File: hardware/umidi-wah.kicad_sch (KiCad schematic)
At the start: 70 parts

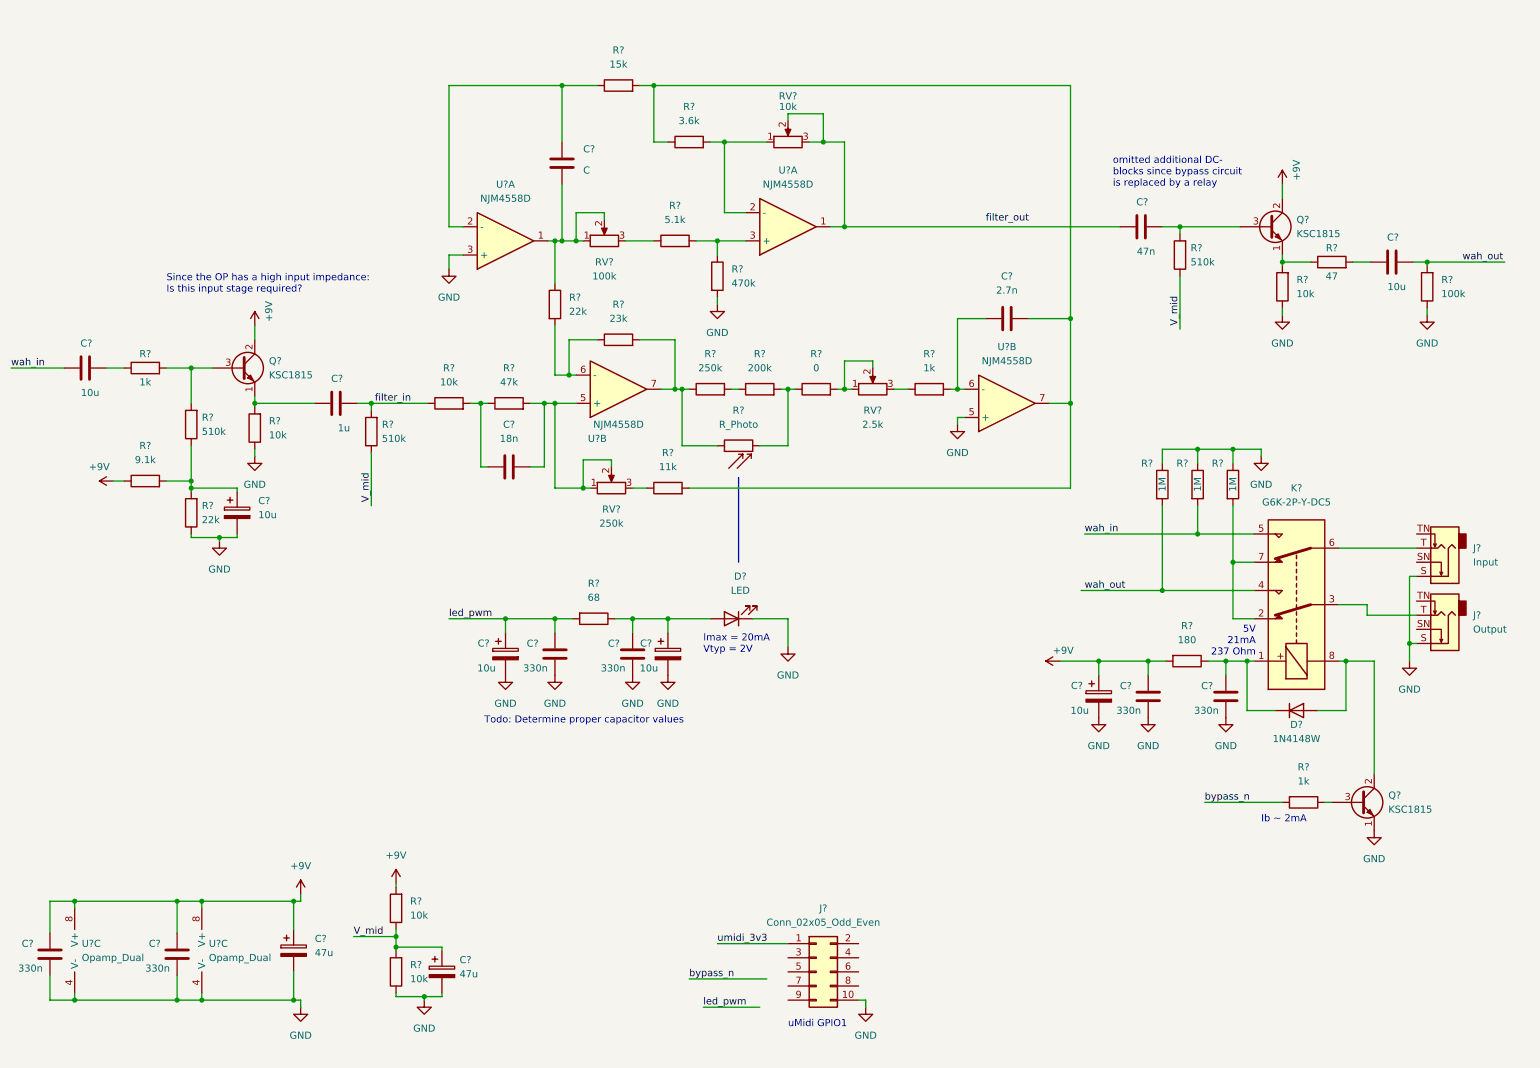
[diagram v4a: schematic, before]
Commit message: Add power input and 5v ldo for umidi supply
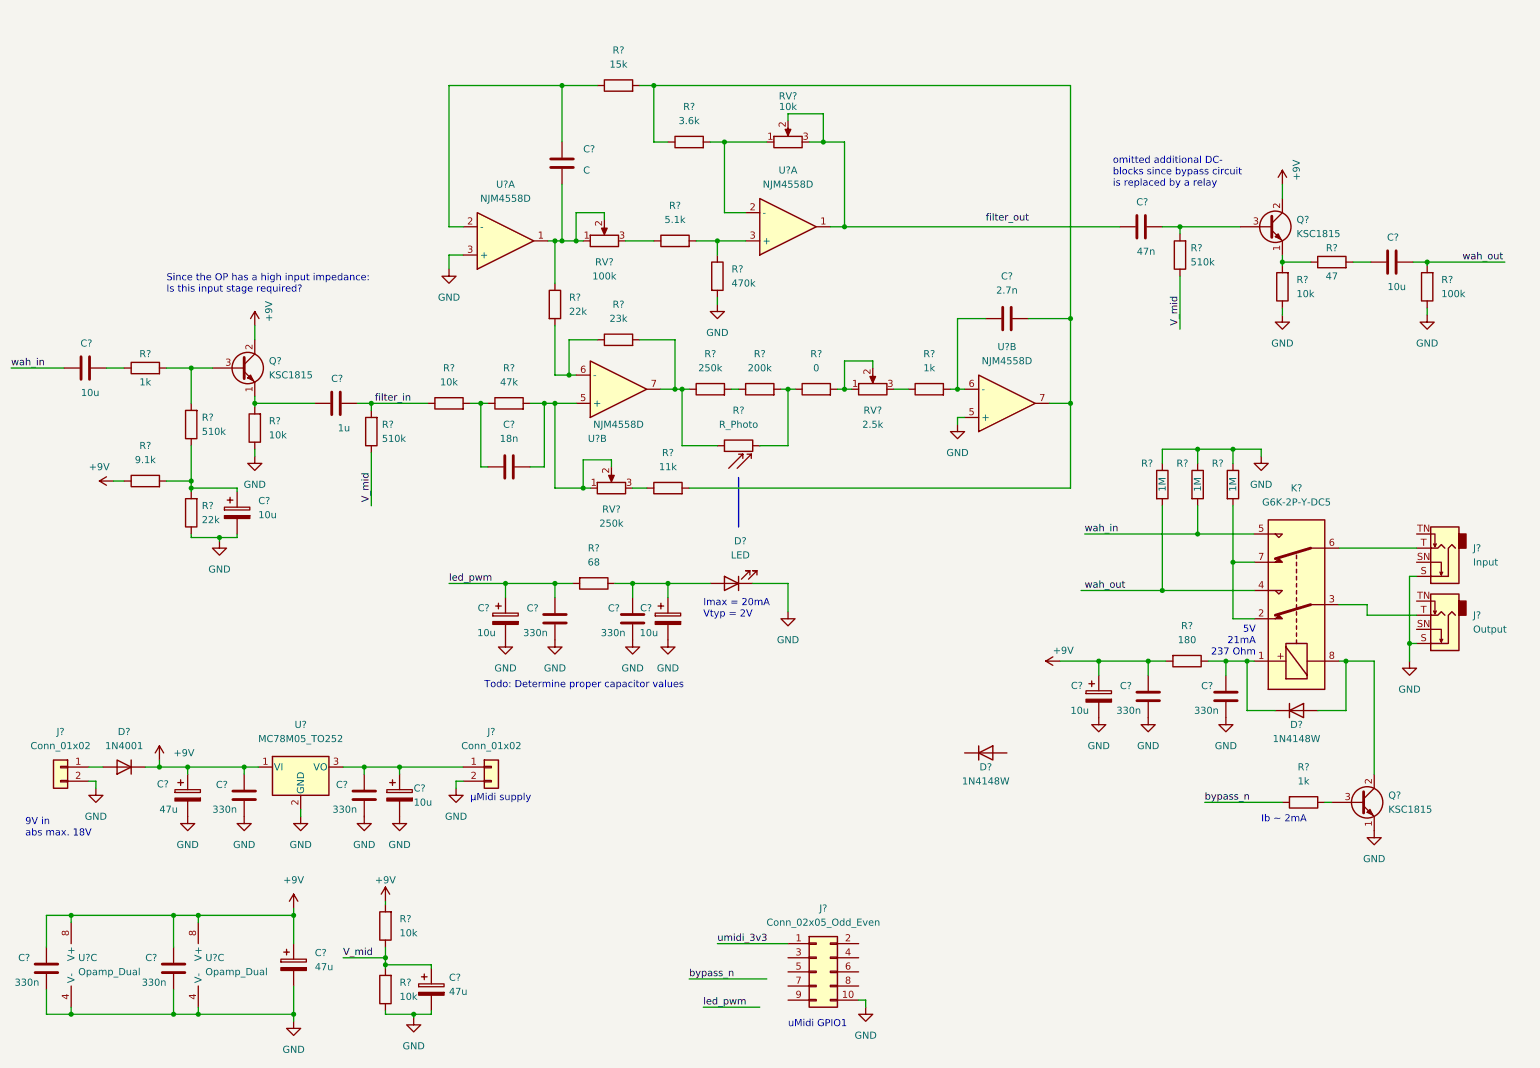
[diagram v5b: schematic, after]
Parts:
- added C? (x2): 330n, symbol Device:C
- added C?: 10u, symbol Device:C_Polarized
- added C?: 47u, symbol Device:C_Polarized
- added D?: 1N4001, Diode_THT:D_DO-41_SOD81_P10.16mm_Horizontal, symbol Diode:1N4001
- added D?: 1N4148W, Diode_SMD:D_SOD-123, symbol Diode:1N4148W
- added J? (x2): Conn_01x02, symbol Connector_Generic:Conn_01x02
- added U?: MC78M05_TO252, Package_TO_SOT_SMD:TO-252-2, symbol Regulator_Linear:MC78M05_TO252
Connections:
- net +9V: now also C?.1, C?.1, D?.1 (K), U?.1 (VI)
- net GND: now also C?.2, C?.2, C?.2, C?.2, J?.2 (Pin_2), J?.2 (Pin_2), U?.2 (GND)
- new net: C?.1, C?.1, J?.1 (Pin_1), U?.3 (VO)
- new net: D?.2 (A), J?.1 (Pin_1)
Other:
- note added: "9V in abs max. 18V"
- note added: "μMidi supply"
- moved on the sheet: C?, D?, R?, U?C

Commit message: Add buffer stage bypass resistors
Can be assembled to bypass input or output buffer stages.
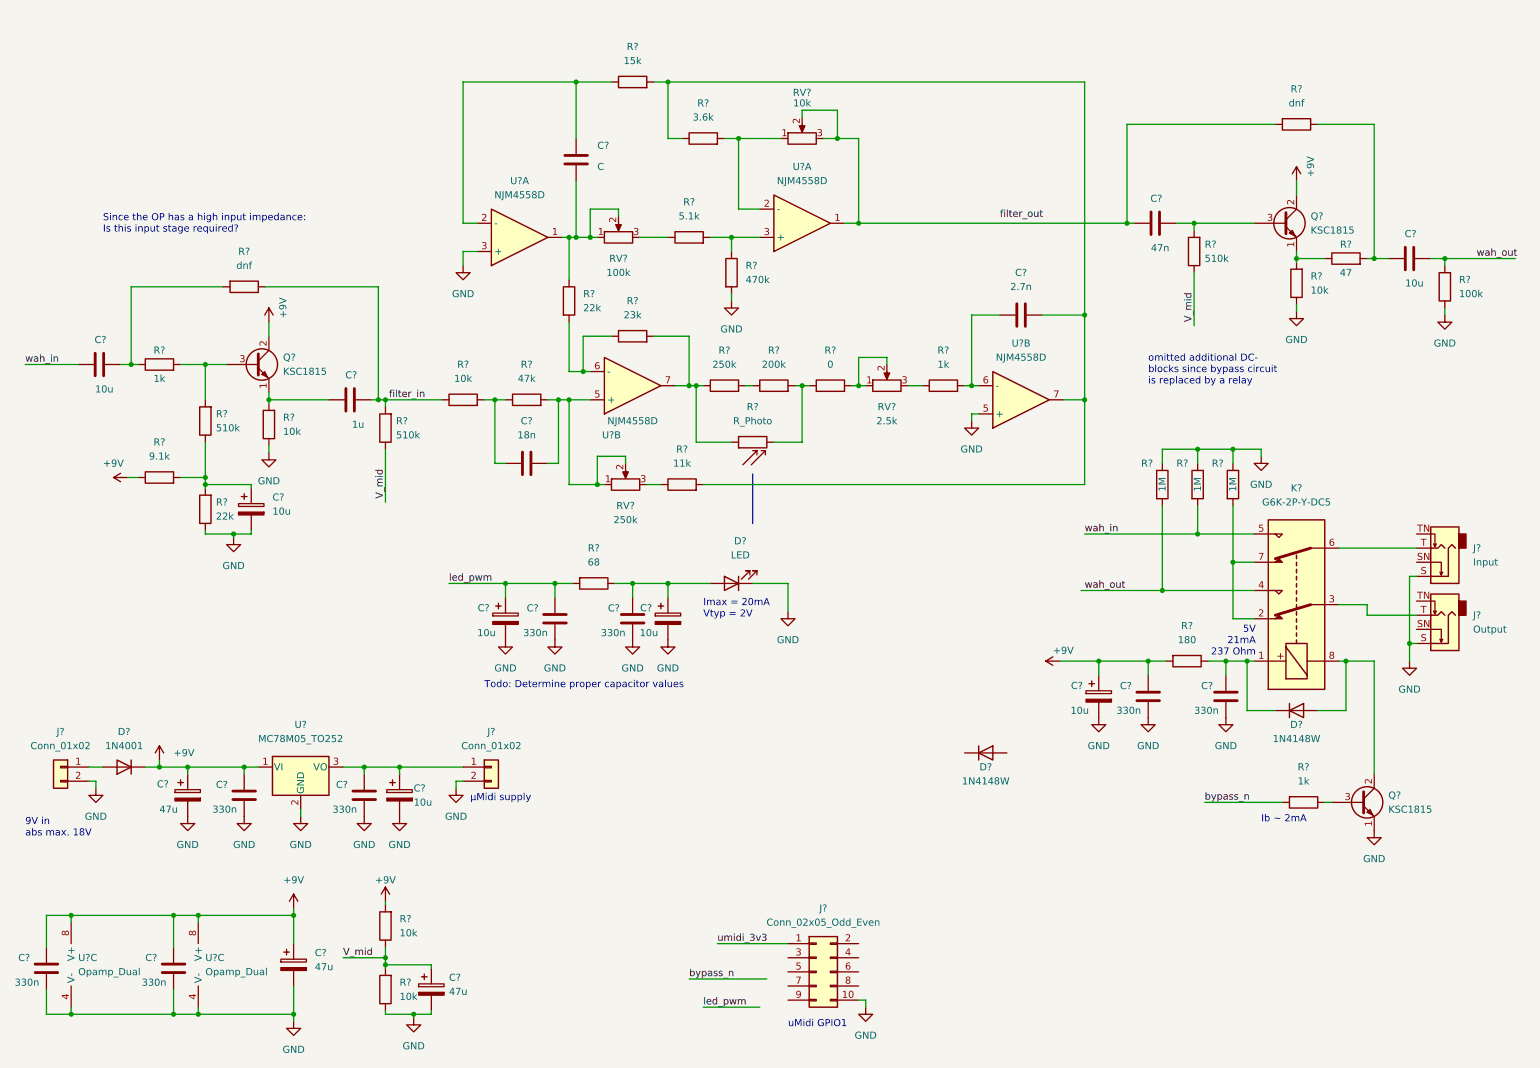
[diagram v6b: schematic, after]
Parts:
- added R? (x2): dnf, symbol Device:R
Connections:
- net filter_in: now also R?.1
- net at C?.1, RV?.2, RV?.3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: now also R?.2
- net at C?.1, R?.2: now also R?.1
- net at C?.2, R?.1: now also R?.2
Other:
- moved on the sheet: C?, Q?, R?, RV?, U?A, U?B

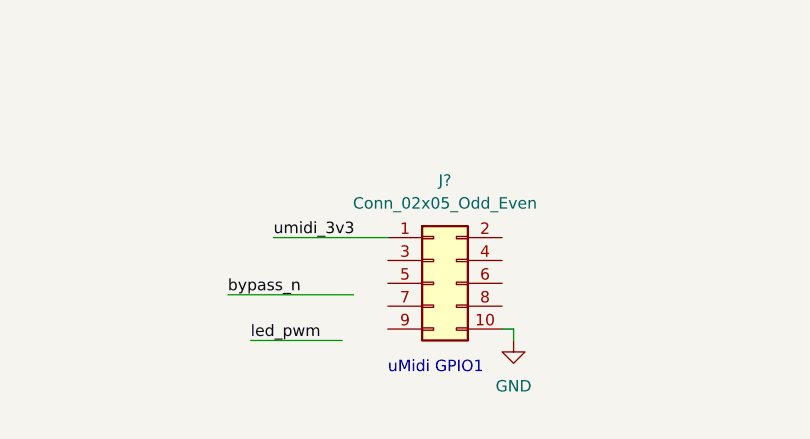
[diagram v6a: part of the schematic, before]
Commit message: Use gpio pinout from current uMidi wah app
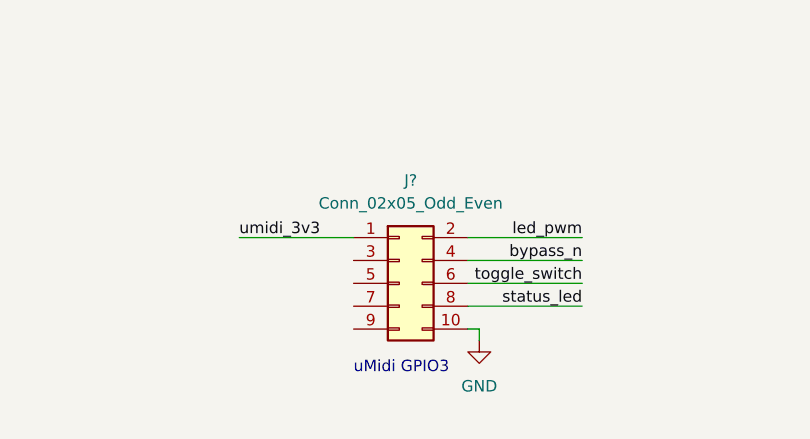
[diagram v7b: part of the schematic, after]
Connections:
- net bypass_n: now also J?.4 (Pin_4)
- net led_pwm: now also J?.2 (Pin_2)
- net toggle_switch: now reaches J?.6 (Pin_6)
- net status_led: now reaches J?.8 (Pin_8)
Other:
- note added: "uMidi GPIO3"
- note removed: "uMidi GPIO1"
- moved on the sheet: J?
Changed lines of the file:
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@@
-    (stroke (width 0) (type default) (color 0 0 0 0))
-  )
-  (wire (pts (xy 134.62 184.15) (xy 148.59 184.15))
     (stroke (width 0) (type default) (color 0 0 0 0))
   )
@@
     (stroke (width 0) (type default) (color 0 0 0 0))
   )
-  (wire (pts (xy 165.1 187.96) (xy 166.37 187.96))
+  (wire (pts (xy 161.29 187.96) (xy 162.56 187.96))
     (stroke (width 0) (type default) (color 0 0 0 0))
   )
@@
     (stroke (width 0) (type default) (color 0 0 0 0))
   )
+  (wire (pts (xy 161.29 185.42) (xy 173.99 185.42))
+    (stroke (width 0) (type default) (color 0 0 0 0))
+  )
   (wire (pts (xy 201.93 80.01) (xy 205.74 80.01))
     (stroke (width 0) (type default) (color 0 0 0 0))
@@
     (stroke (width 0) (type default) (color 0 0 0 0))
   )
-  (wire (pts (xy 137.16 189.23) (xy 147.32 189.23))
-    (stroke (width 0) (type default) (color 0 0 0 0))
-  )
   (wire (pts (xy 264.16 111.76) (xy 264.16 123.825))
     (stroke (width 0) (type default) (color 0 0 0 0))
@@
     (stroke (width 0) (type default) (color 0 0 0 0))
   )
+  (wire (pts (xy 161.29 182.88) (xy 173.99 182.88))
+    (stroke (width 0) (type default) (color 0 0 0 0))
+  )
   (wire (pts (xy 52.705 104.14) (xy 55.88 104.14))
     (stroke (width 0) (type default) (color 0 0 0 0))
@@
     (stroke (width 0) (type default) (color 0 0 0 0))
   )
-  (wire (pts (xy 139.7 177.8) (xy 152.4 177.8))
+  (wire (pts (xy 135.89 177.8) (xy 148.59 177.8))
     (stroke (width 0) (type default) (color 0 0 0 0))
   )
@@
     (stroke (width 0) (type default) (color 0 0 0 0))
   )
+  (wire (pts (xy 161.29 180.34) (xy 173.99 180.34))
+    (stroke (width 0) (type default) (color 0 0 0 0))
+  )
   (wire (pts (xy 114.3 22.86) (xy 114.3 33.02))
     (stroke (width 0) (type default) (color 0 0 0 0))
@@
     (stroke (width 0) (type default) (color 0 0 0 0))
   )
-  (wire (pts (xy 166.37 187.96) (xy 166.37 189.23))
+  (wire (pts (xy 162.56 187.96) (xy 162.56 189.23))
     (stroke (width 0) (type default) (color 0 0 0 0))
   )
@@
   )
   (wire (pts (xy 144.78 77.47) (xy 146.05 77.47))
+    (stroke (width 0) (type default) (color 0 0 0 0))
+  )
+  (wire (pts (xy 161.29 177.8) (xy 173.99 177.8))
     (stroke (width 0) (type default) (color 0 0 0 0))
   )
@@
     (effects (font (size 1.27 1.27)) (justify left bottom))
   )
-  (text "uMidi GPIO1" (at 152.4 193.04 0)
+  (text "uMidi GPIO3" (at 148.59 193.04 0)
     (effects (font (size 1.27 1.27)) (justify left bottom))
   )
@@
     (effects (font (size 1.27 1.27)) (justify left bottom))
   )
+  (label "toggle_switch" (at 173.99 182.88 180)
+    (effects (font (size 1.27 1.27)) (justify right bottom))
+  )
   (label "wah_in" (at 15.24 73.66 0)
     (effects (font (size 1.27 1.27)) (justify left bottom))
   )
+  (label "status_led" (at 173.99 185.42 180)
+    (effects (font (size 1.27 1.27)) (justify right bottom))
+  )
   (label "filter_in" (at 80.645 80.01 0)
     (effects (font (size 1.27 1.27)) (justify left bottom))
@@
     (effects (font (size 1.27 1.27)) (justify left bottom))
   )
-  (label "umidi_3v3" (at 139.7 177.8 0)
+  (label "umidi_3v3" (at 135.89 177.8 0)
     (effects (font (size 1.27 1.27)) (justify left bottom))
   )
-  (label "led_pwm" (at 137.16 189.23 0)
-    (effects (font (size 1.27 1.27)) (justify left bottom))
+  (label "led_pwm" (at 173.99 177.8 180)
+    (effects (font (size 1.27 1.27)) (justify right bottom))
   )
   (label "filter_out" (at 190.5 47.625 0)
     (effects (font (size 1.27 1.27)) (justify left bottom))
   )
-  (label "bypass_n" (at 134.62 184.15 0)
-    (effects (font (size 1.27 1.27)) (justify left bottom))
+  (label "bypass_n" (at 173.99 180.34 180)
+    (effects (font (size 1.27 1.27)) (justify right bottom))
   )
   (label "V_mid" (at 225.425 66.04 90)
@@
     (pin "2")
   )
-  (symbol (lib_id "Connector_Generic:Conn_02x05_Odd_Even") (at 157.48 182.88 0) (unit 1)
-    (in_bom yes) (on_board yes) (fields_autoplaced)
-    (property "Reference" "J?" (id 0) (at 158.75 171.45 0))
-    (property "Value" "Conn_02x05_Odd_Even" (id 1) (at 158.75 173.99 0))
-    (property "Footprint" "Connector_IDC:IDC-Header_2x05_P2.54mm_Vertical" (id 2) (at 157.48 182.88 0)
-      (effects (font (size 1.27 1.27)) hide)
-    )
-    (property "Datasheet" "~" (id 3) (at 157.48 182.88 0)
+  (symbol (lib_id "Connector_Generic:Conn_02x05_Odd_Even") (at 153.67 182.88 0) (unit 1)
+    (in_bom yes) (on_board yes) (fields_autoplaced)
+    (property "Reference" "J?" (id 0) (at 154.94 171.45 0))
+    (property "Value" "Conn_02x05_Odd_Even" (id 1) (at 154.94 173.99 0))
+    (property "Footprint" "Connector_IDC:IDC-Header_2x05_P2.54mm_Vertical" (id 2) (at 153.67 182.88 0)
+      (effects (font (size 1.27 1.27)) hide)
+    )
+    (property "Datasheet" "~" (id 3) (at 153.67 182.88 0)
       (effects (font (size 1.27 1.27)) hide)
     )
@@
     (pin "2")
   )
-  (symbol (lib_id "power:GND") (at 166.37 189.23 0) (unit 1)
-    (in_bom yes) (on_board yes) (fields_autoplaced)
-    (property "Reference" "#PWR?" (id 0) (at 166.37 195.58 0)
-      (effects (font (size 1.27 1.27)) hide)
-    )
-    (property "Value" "GND" (id 1) (at 166.37 194.31 0))
-    (property "Footprint" "" (id 2) (at 166.37 189.23 0)
-      (effects (font (size 1.27 1.27)) hide)
-    )
-    (property "Datasheet" "" (id 3) (at 166.37 189.23 0)
-      (effects (font (size 1.27 1.27)) hide)
-    )
+  (symbol (lib_id "power:GND") (at 162.56 189.23 0) (unit 1)
+    (in_bom yes) (on_board yes) (fields_autoplaced)
+    (property "Reference" "#PWR?" (id 0) (at 162.56 195.58 0)
+      (effects (font (size 1.27 1.27)) hide)
+    )
+    (property "Value" "GND" (id 1) (at 162.56 194.31 0))
+    (property "Footprint" "" (id 2) (at 162.56 189.23 0)
+      (effects (font (size 1.27 1.27)) hide)
+    )
+    (property "Datasheet" "" (id 3) (at 162.56 189.23 0)
+      (effects (font (size 1.27 1.27)) hide)
+    )

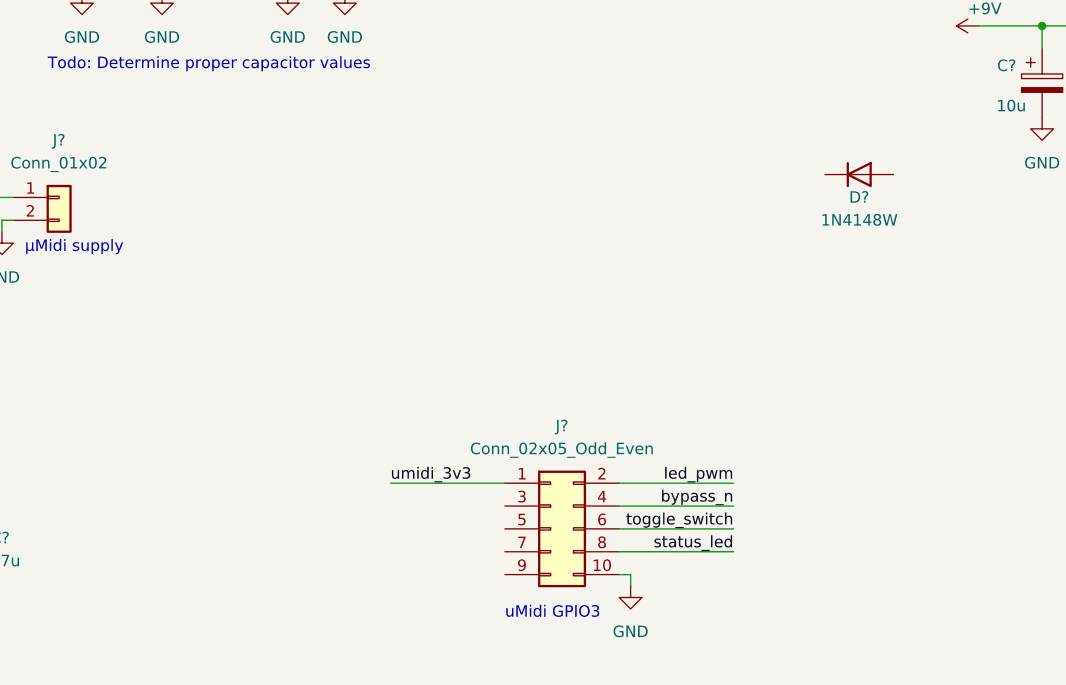
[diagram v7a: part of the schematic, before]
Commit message: Add status led and toggle switch connector
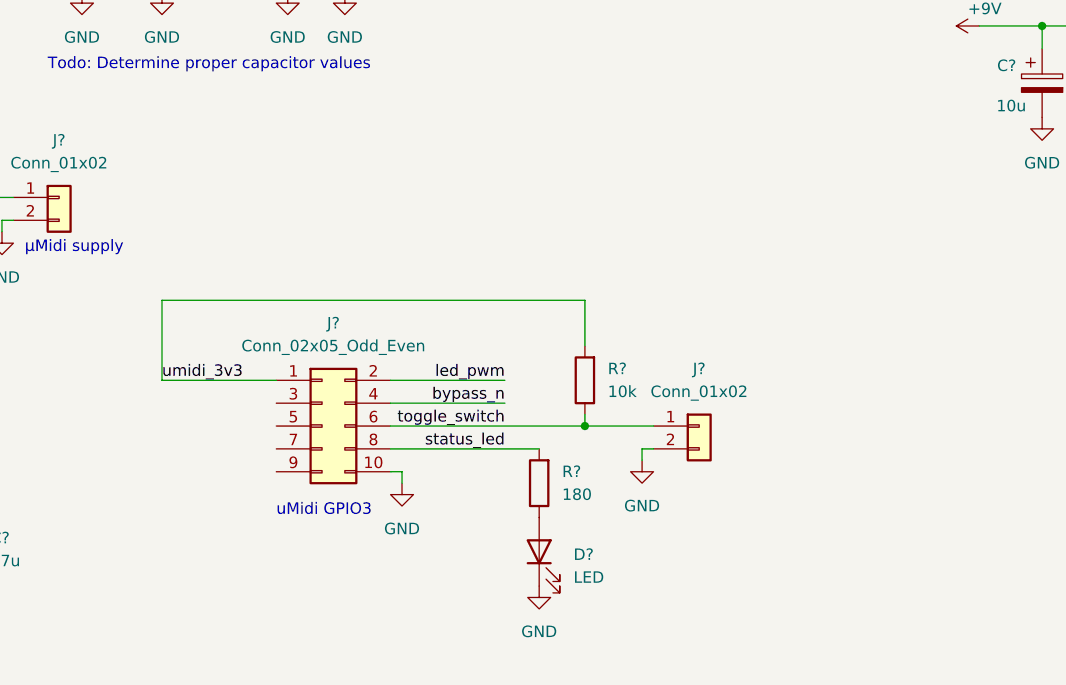
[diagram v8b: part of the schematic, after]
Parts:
- removed D?: 1N4148W, Diode_SMD:D_SOD-123, symbol Diode:1N4148W
- added D?: LED, symbol Device:LED
- added J?: Conn_01x02, symbol Connector_Generic:Conn_01x02
- added R?: 180, symbol Device:R
- added R?: 10k, symbol Device:R
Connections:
- net GND: now also D?.1 (K), J?.2 (Pin_2)
- net status_led: now also R?.2
- net toggle_switch: now also J?.1 (Pin_1), R?.1
- net umidi_3v3: now also R?.2
- new net: D?.2 (A), R?.1
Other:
- moved on the sheet: J?
